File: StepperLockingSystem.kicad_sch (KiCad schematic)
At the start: 18 parts, among them J1 Conn_12V, U1 INA180A1, U2 TC1185

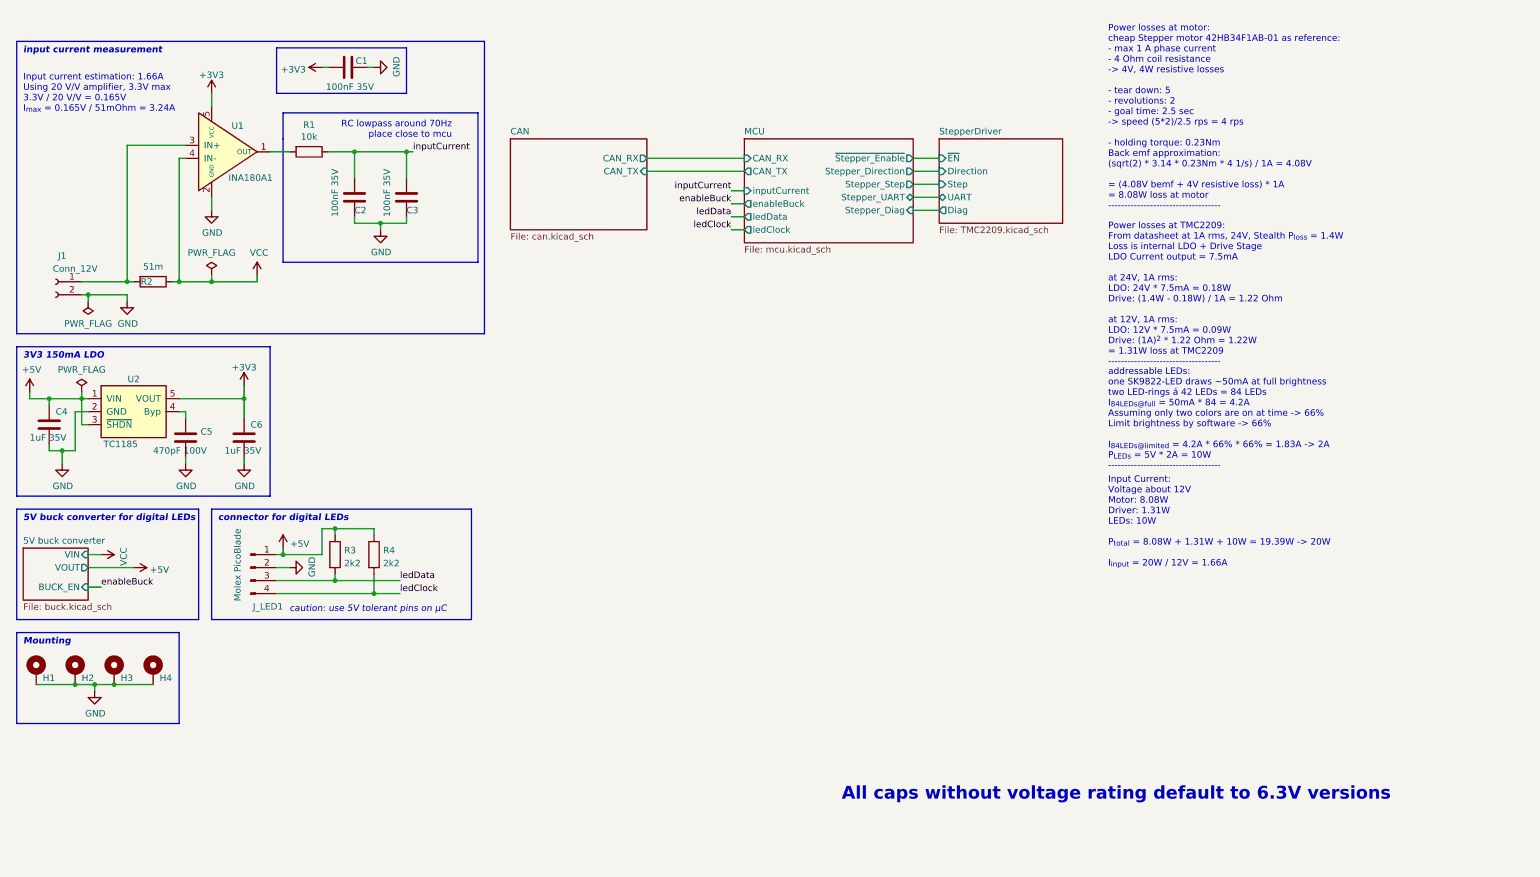
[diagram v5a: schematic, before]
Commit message: Add many changes to schematic and WIP PCB
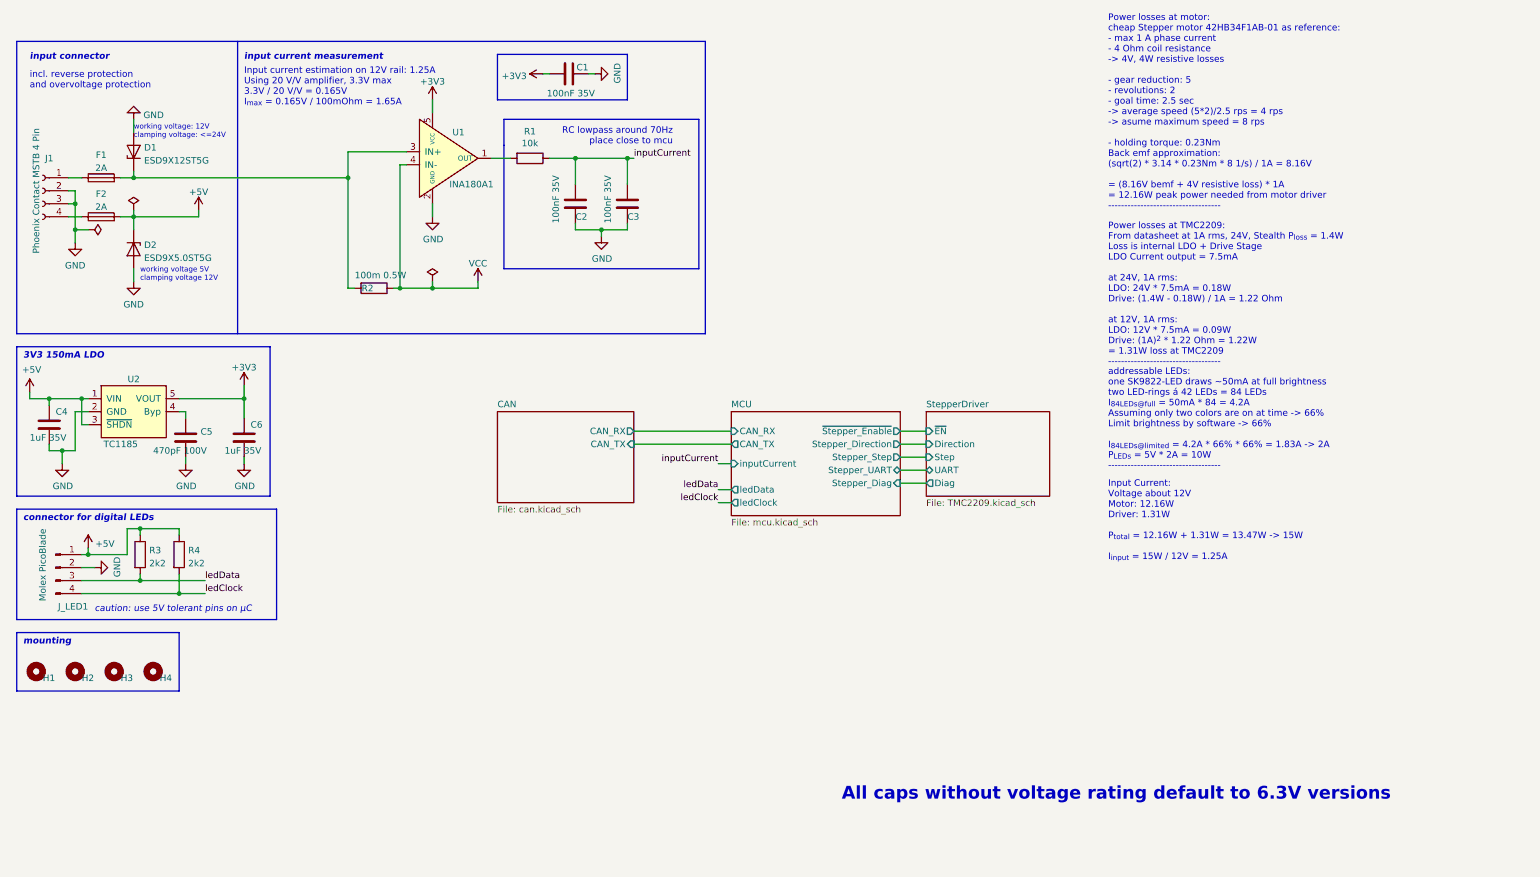
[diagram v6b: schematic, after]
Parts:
- removed J1: Conn_12V, Connector_AMASS:AMASS_XT30U-M_1x02_P5.0mm_Vertical, symbol Connector:Conn_01x02_Female
- added D1: ESD9X12ST5G, Diode_SMD:D_SOD-923, symbol Device:D_Zener
- added D2: ESD9X5.0ST5G, Diode_SMD:D_SOD-923, symbol Device:D_Zener
- added F1, F2: 2A, extraFootprints:KEYSTONE-FUSE-3557-2, symbol Device:Fuse
- added J1: Phoenix Contact MSTB 4 Pin, Connector_Phoenix_MSTB:PhoenixContact_MSTBVA_2,5_4-G-5,08_1x04_P5.08mm_Vertical, symbol Connector:Conn_01x04_Female
- H1, H2, H3, H4: footprint MountingHole:MountingHole_3.2mm_M3_Pad_Via -> MountingHole:MountingHole_3.2mm_M3_ISO14580; symbol Mechanical:MountingHole_Pad -> Mechanical:MountingHole
- R2: value 51m -> 100m 0.5W
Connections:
- net +5V: now also D2.1 (K), F2.2
- net GND: now also D1.2 (A), D2.2 (A), J1.2 (Pin_2), J1.3 (Pin_3); no longer H1.1, H2.1, H3.1, H4.1
- net at R2.2, U1.3 (IN+): now also D1.1 (K), F1.2
- new net: F1.1, J1.1 (Pin_1)
- new net: F2.1, J1.4 (Pin_4)
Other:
- removed sheet 5V buck converter
- sheet MCU ports: added none; removed enableBuck
- note added: "Input Current: Voltage about 12V Motor: 12.16W Driver: 1.31W P_{total} = 12.16W + 1.31W = 13.47W -> 15W I_{input} = 15W / 12V = 1.25A"
- note added: "Input current estimation on 12V rail: 1.25A Using 20 V/V amplifier, 3.3V max 3.3V / 20 V/V = 0.165V I_{max} = 0.165V / 100mOhm = 1.65A"
- note added: "Power losses at motor: cheap Stepper motor 42HB34F1AB-01 as reference: - max 1 A phase current - 4 Ohm coil resistance -> 4V, 4W resistive losses - gear reduction: 5 - revolutions: 2 - goal time: 2.5 sec -> average speed (5*2)/2.5 rps = 4 rps -> asume maximum speed = 8 rps - holding torque: 0.23Nm Back emf approximation: (sqrt(2) * 3.14 * 0.23Nm * 8 1/s) / 1A = 8.16V = (8.16V bemf + 4V resistive 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"
- note added: "incl. reverse protection and overvoltage protection"
- note added: "input connector"
- note added: "mounting"
- note added: "working voltage 5V clamping voltage 12V"
- note added: "working voltage: 12V clamping voltage: <=24V"
- note removed: "5V buck converter for digital LEDs"
- note removed: "Input Current: Voltage about 12V Motor: 8.08W Driver: 1.31W LEDs: 10W P_{total} = 8.08W + 1.31W + 10W = 19.39W -> 20W I_{input} = 20W / 12V = 1.66A"
- note removed: "Input current estimation: 1.66A Using 20 V/V amplifier, 3.3V max 3.3V / 20 V/V = 0.165V I_{max} = 0.165V / 51mOhm = 3.24A"
- note removed: "Mounting"
- note removed: "Power losses at motor: cheap Stepper motor 42HB34F1AB-01 as reference: - max 1 A phase current - 4 Ohm coil resistance -> 4V, 4W resistive losses - tear down: 5 - revolutions: 2 - goal time: 2.5 sec -> speed (5*2)/2.5 rps = 4 rps - holding torque: 0.23Nm Back emf approximation: (sqrt(2) * 3.14 * 0.23Nm * 4 1/s) / 1A = 4.08V = (4.08V bemf + 4V resistive loss) * 1A = 8.08W loss at motor -----------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"
- moved on the sheet: C1, C2, C3, J_LED1, R1, R2, R3, R4, U1

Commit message: Some changes to schematic
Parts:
- C1, C2, C3: value 100nF 35V -> 100nF
- C4, C6: value 1uF 35V -> 1uF
- C5: value 470pF 100V -> 470pF
- F1: value 2A -> 12V 2A
- F2: value 2A -> 5V 2A
- J1: value Phoenix Contact MSTB 4 Pin -> PowerConnector
- J_LED1: value Molex PicoBlade -> DigitalLED
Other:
- moved on the sheet: C1, C2, C3, H1, H2, H3, H4, R1, R2, U1

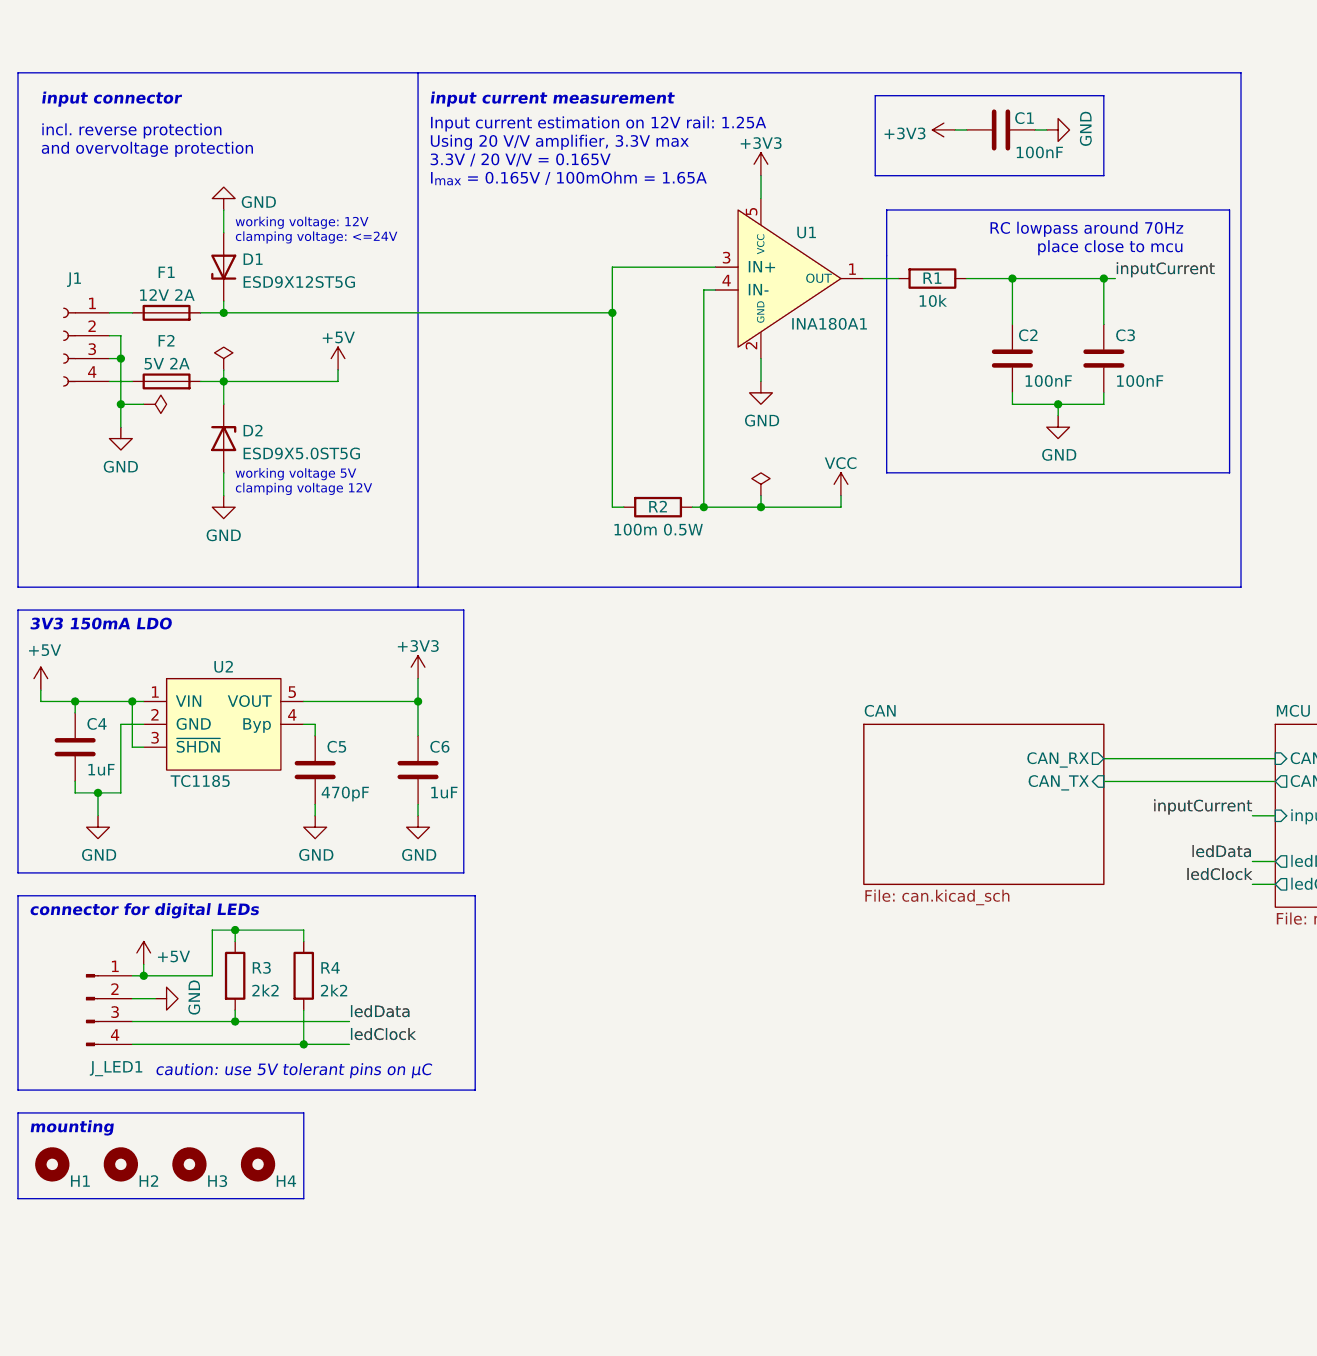
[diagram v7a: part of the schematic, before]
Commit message: Finish PCB layout
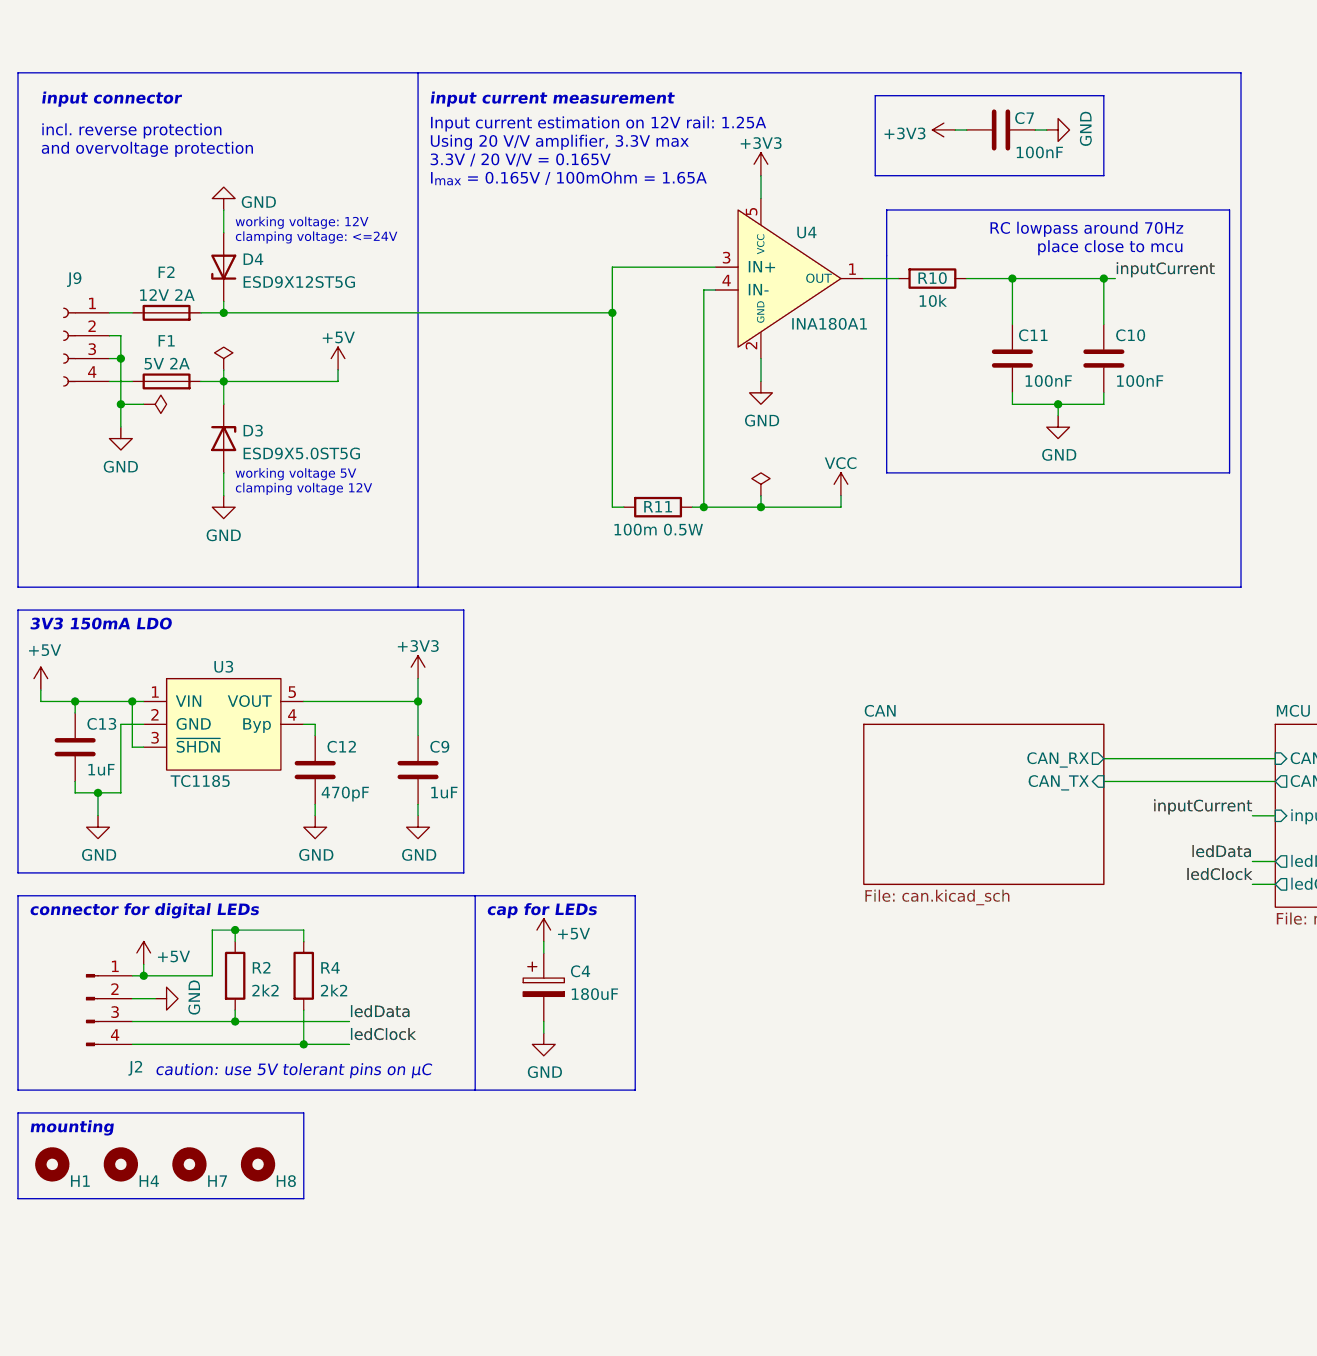
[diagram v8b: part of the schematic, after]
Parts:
- added C4: 180uF, Capacitor_THT:CP_Radial_D7.5mm_P2.50mm, symbol Device:C_Polarized
- H1: footprint MountingHole:MountingHole_3.2mm_M3_ISO14580 -> extraFootprints:MountingHole_3.2mm_M3_ISO7380_Keepout
- H4: renamed from H2; footprint MountingHole:MountingHole_3.2mm_M3_ISO14580 -> extraFootprints:MountingHole_3.2mm_M3_ISO7380_Keepout
- H7: renamed from H3; footprint MountingHole:MountingHole_3.2mm_M3_ISO14580 -> extraFootprints:MountingHole_3.2mm_M3_ISO7380_Keepout
- H8: renamed from H4; footprint MountingHole:MountingHole_3.2mm_M3_ISO14580 -> extraFootprints:MountingHole_3.2mm_M3_ISO7380_Keepout
- renumbered C3 to C10, C2 to C11, C5 to C12, C4 to C13, C1 to C7, C6 to C9, D2 to D3, D1 to D4, F2 to F1, F1 to F2, J_LED1 to J2, J1 to J9, R1 to R10, R2 to R11, R3 to R2, U2 to U3, U1 to U4
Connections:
- net +5V: now also C4.1
- net GND: now also C4.2
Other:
- note added: "cap for LEDs"
